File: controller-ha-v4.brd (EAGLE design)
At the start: 120 x 71 mm, 45 parts, among them J2 COMPUTER-PERIPHERAL-POWERRA, U1 DS1307, U3 ARDUINO-MEGAFULL

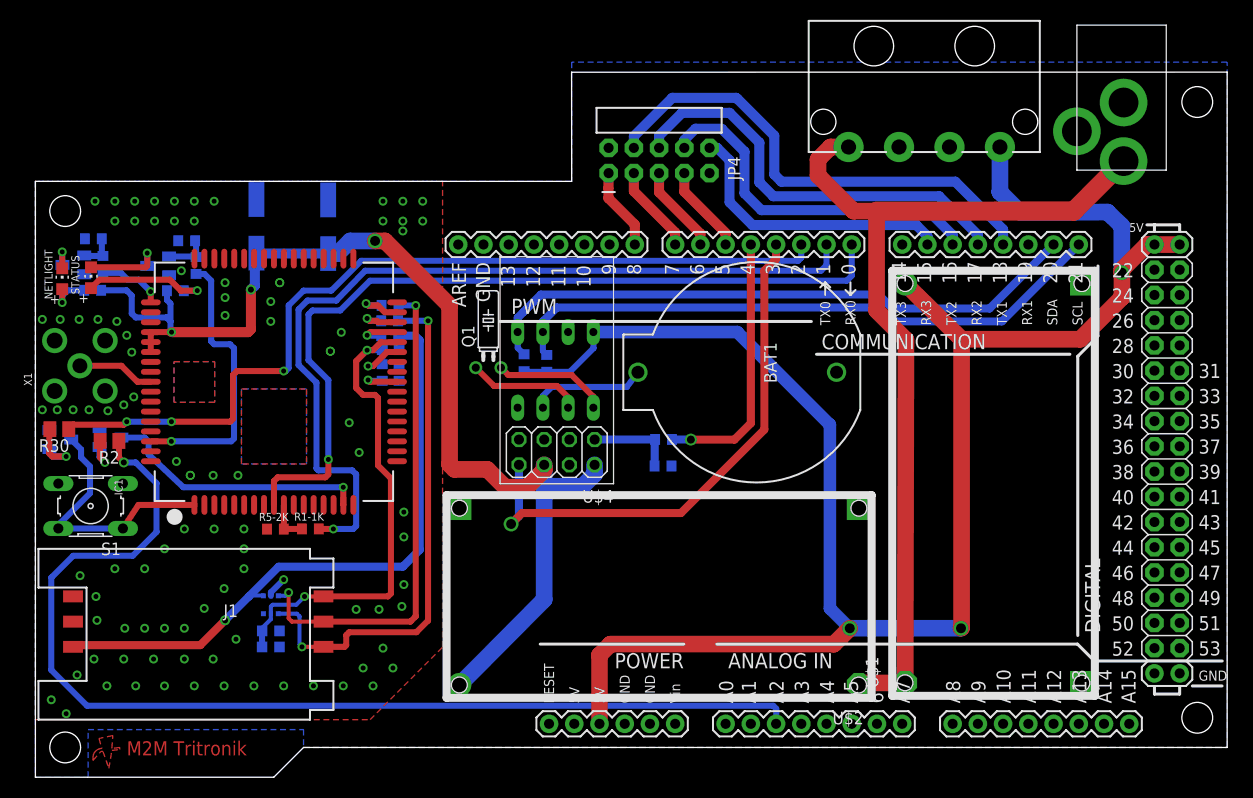
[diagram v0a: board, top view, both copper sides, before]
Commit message: Submit all new design
Adding version 3-4 for driver & controller; Adding version 1-2 IO Module
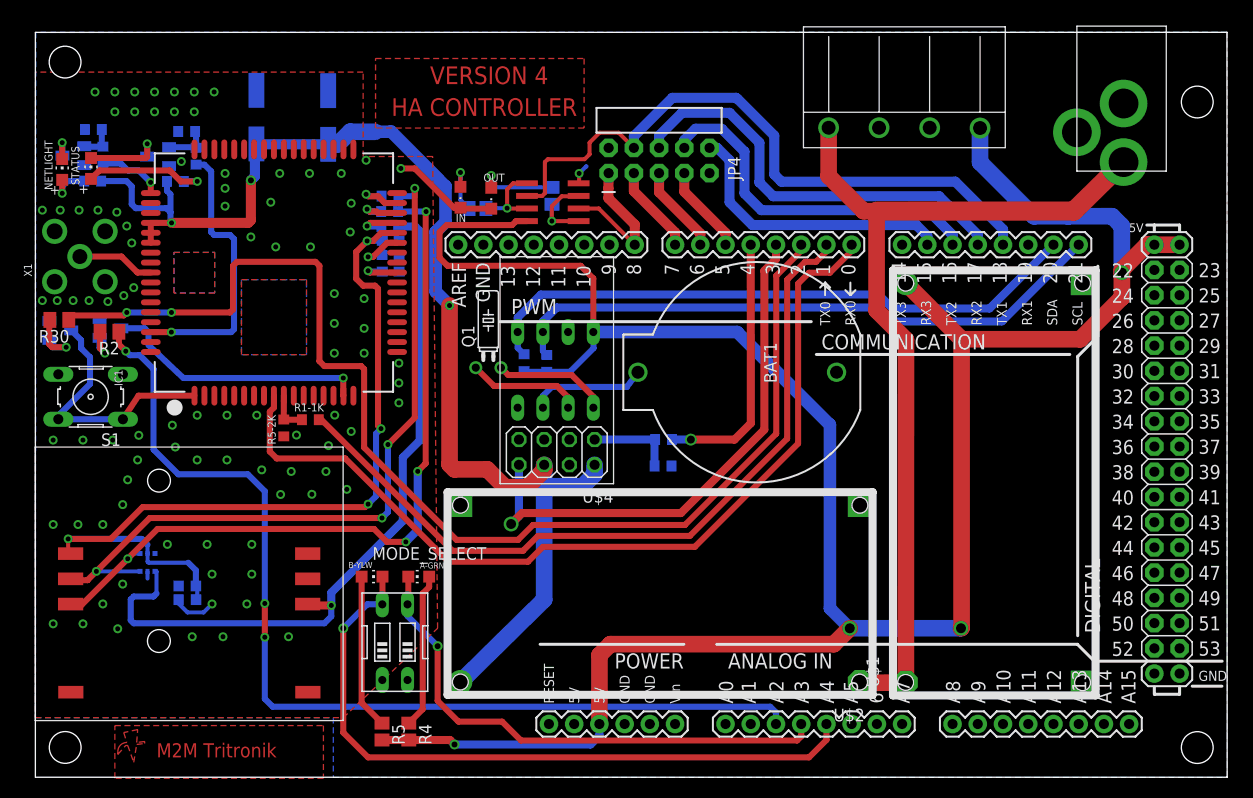
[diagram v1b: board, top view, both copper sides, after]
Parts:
- removed J1: (no value), SparkFun-Connectors:SIMHOLDER
- removed J2: COMPUTER-PERIPHERAL-POWERRA, SparkFun-Connectors:COMPUTER-PERIPHERAL-POWER-RA
- added A-GRN, B-YLW: (no value), led:CHIP-LED0805
- added IC2: LM358MX, linear:SO08
- added IN, OUT: (no value), adafruit:CHIPLED_0805
- added MODE_SELECT: (no value), special:EDG-02
- added R1, R3, R4, R5: (no value), resistor:R0805
- added U$5: SIM_HOLDER_PUSH, maul:SIM_HOLDER_PUSH
- added U$6: 4-PIN-CON-1759017, maul:4-PIN-CON-1759017
- moved U3 60.8 mm to (73.3, 29.5)
- moved D15 13.1 mm to (11.3, 21.6), turned to 0 degrees
- moved C8-100U 11.0 mm to (29.5, 66.4)
- moved S1 11.0 mm to (5.56, 38.3)
- moved C10-4U7 11.0 mm to (35.8, 50.9)
- moved C11-22P 11.0 mm to (35.8, 52.6)
- moved C7-100U 11.0 mm to (22.3, 66.5)
- moved C9-100N 11.0 mm to (35.8, 54.0)
- moved IC1 11.0 mm to (24.0, 50.8)
- moved NETLIGHT 11.0 mm to (2.70, 61.2)
- moved R1-1K 11.0 mm to (27.7, 36.0)
- moved R10-22 11.0 mm to (35.7, 57.0)
- moved R11-22 11.0 mm to (35.7, 55.5)
- moved R2 11.0 mm to (7.46, 44.9)
- moved R20-1K 11.0 mm to (14.1, 60.0)
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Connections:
- new net N$21: IC2.1, IC2.3, R1.1
- new net N$24: IC2.5, IC2.7, R3.1
- new net N$25: OUT.A, R1.2
- new net N$26: IN.A, R3.2
- new net N$27: A-GRN.A, R4.1
- new net N$28: B-YLW.A, R5.1
- new net STATE_A: A-GRN.C, MODE_SELECT.3, U3.A3
- new net STATE_B: B-YLW.C, MODE_SELECT.4, U3.A4
- net +12V: now also U$6.4; no longer J2.5V
- net GND: now also IC2.4, IN.C, MODE_SELECT.1, MODE_SELECT.2, OUT.C, U$5.GND, U$6.2, U$6.3; no longer J1.C5, J2.GND, J2.NC
- net Q7: now also IC2.2
- net SR_DS: now also IC2.6
- net USIM_CLK: now also U$5.CLK; no longer J1.C3
- net USIM_DATA: now also U$5.I/O; no longer J1.C7
- net USIM_RESET: now also U$5.RST; no longer J1.C2
- net USIM_VCC: now also U$5.VCC; no longer J1.C1
- net VCC: now also IC2.8, R4.2, R5.2, U$6.1; no longer J2.12V
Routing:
- net STATE_B: track 0.00 -> 70.3 mm, vias 0 -> 1
- net VCC: track 190.7 -> 250.0 mm, vias 3 -> 4
- net STATE_A: track 0.00 -> 53.5 mm, vias 0 -> 1
- net USIM_VCC: track 50.5 -> 87.4 mm, vias 2 -> 4
- net PWRKEY: track 88.5 -> 122.6 mm, vias 3 -> 2
- net USIM_RESET: track 50.5 -> 76.0 mm, vias 2 -> 4
- net USIM_CLK: track 53.0 -> 75.9 mm, vias 2 -> 4
- net SR_DS: track 49.2 -> 65.8 mm
- net GND: track 5.67 -> 21.5 mm, vias 98 -> 94
- net N$28: track 0.00 -> 15.6 mm
- net N$27: track 0.00 -> 15.6 mm
- net +3V3: track 116.5 -> 128.4 mm
- net USIM_DATA: track 64.0 -> 75.8 mm
- net N$21: track 0.00 -> 9.03 mm, vias 0 -> 1
- net CTRL_SIMRESET: track 109.4 -> 100.9 mm, vias 1 -> 3
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- added copper zone on layer 1, net N$18
- added copper zone on layer 1, net N$22
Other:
- board size 120 x 71 mm -> 120 x 75 mm
- board text added: "HA CONTROLLER"
- board text added: "VERSION 4"

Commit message: change in controller design
Change component position & adding hole to controller design
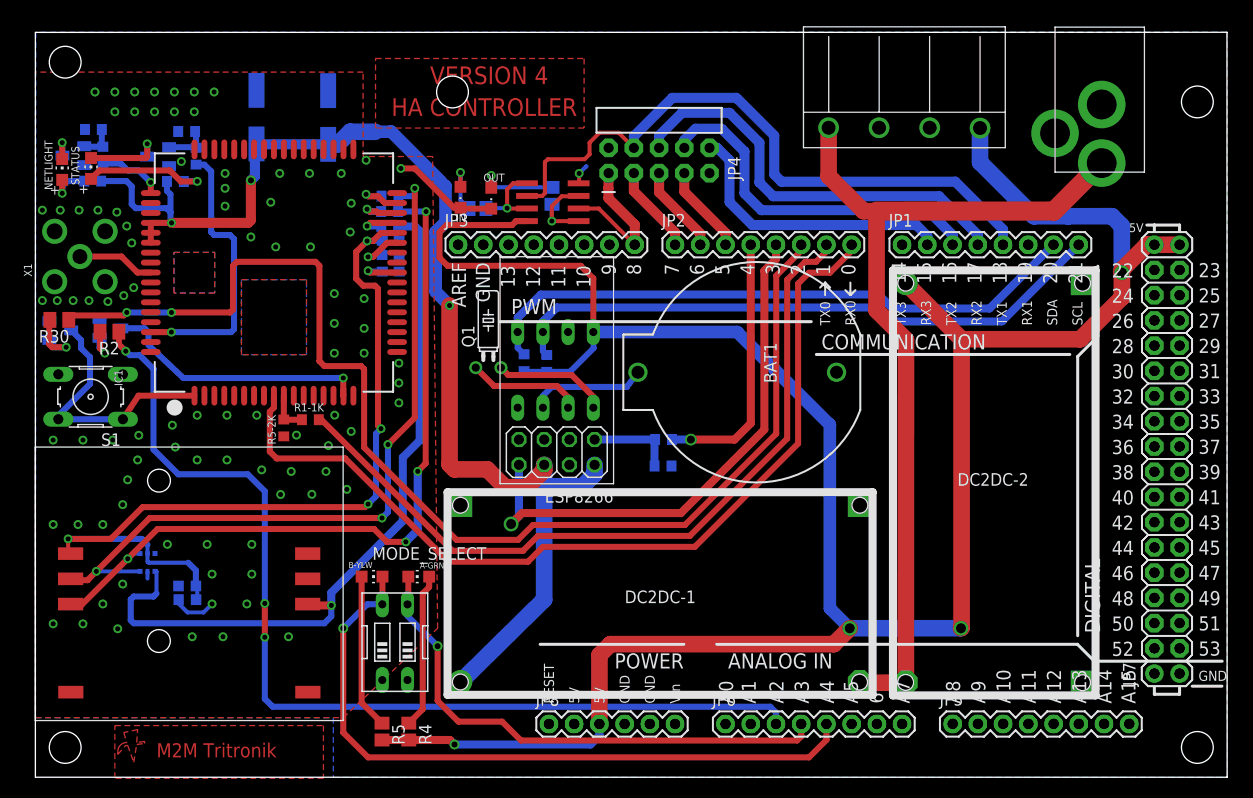
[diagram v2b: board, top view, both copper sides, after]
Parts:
- removed U$3: 2.1MMJACKTHM, adafruit:PJ-102A
- added DC_JACKTHM: 2.1MMJACKTHM, adafruit:PJ-102A
- added JP1, JP2, JP3, JP5, JP6: (no value), adafruit:1X08-CLEANBIG
- added JP7: (no value), pinhead:2X18
- added JP8: (no value), adafruit:1X06-CLEANBIG
- A-GRN, IN, NETLIGHT, OUT: value (none) -> green
- B-YLW, STATUS: value (none) -> yellow
- C10-4U7: value (none) -> 4.7nF
- C11, CSIM_22P: value (none) -> 22pF
- C7-100U, C8-100U: value (none) -> 100uF
- C9, CSIM_100N: value (none) -> 100nF
- R1, R3: value (none) -> 220
- R1-1K, R1-1K1, R20-1K, R23-1K, R26-1K, R27-1K, R4, R5: value (none) -> 1K
- R10-22, R11-22, R9-22: value (none) -> 22
- R2, R30: value R120 -> 120
- R25-10K, R28-10K: value (none) -> 10K
- R2K2_SCL, R2K2_SDA: value (none) -> 2.2K
- R5-2K, R5-2K1: value (none) -> 2K
- renumbered C11-22P to C11, C9-100N to C9, U$1 to DC2DC-2, U$2 to DC2DC-1, U$4 to ESP8266, U$5 to SIM_HOLDER, U$6 to 4-WAY_L-TERMINAL, U3 to ARDUINO_FOOTPRINT
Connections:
- net +12V: now also DC_JACKTHM.TIP; no longer U$3.TIP
- net GND: now also DC_JACKTHM.RING, DC_JACKTHM.RING_SW; no longer U$3.RING, U$3.RING_SW
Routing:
- net +12V: track 91.4 -> 89.2 mm
